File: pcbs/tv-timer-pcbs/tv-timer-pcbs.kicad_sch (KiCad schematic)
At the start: 9 parts, among them J1 Conn_01x03, J2 Conn_01x03

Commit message: Digit ready to go
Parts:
- D1, D2, D3, D4, D5, D6, D7: footprint ProjectLibrary:WS2812b_5mm_THT -> LED_THT:LED_D5.0mm-4_RGB_Wide_Pins
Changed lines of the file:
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@@
 			)
 		)
-		(property "Footprint" "ProjectLibrary:WS2812b_5mm_THT"
+		(property "Footprint" "LED_THT:LED_D5.0mm-4_RGB_Wide_Pins"
 			(at 86.36 57.15 0)
 			(hide yes)
@@
 			)
 		)
-		(property "Footprint" "ProjectLibrary:WS2812b_5mm_THT"
+		(property "Footprint" "LED_THT:LED_D5.0mm-4_RGB_Wide_Pins"
 			(at 193.04 57.15 0)
 			(hide yes)
@@
 			)
 		)
-		(property "Footprint" "ProjectLibrary:WS2812b_5mm_THT"
+		(property "Footprint" "LED_THT:LED_D5.0mm-4_RGB_Wide_Pins"
 			(at 137.16 57.15 0)
 			(hide yes)
@@
 			)
 		)
-		(property "Footprint" "ProjectLibrary:WS2812b_5mm_THT"
+		(property "Footprint" "LED_THT:LED_D5.0mm-4_RGB_Wide_Pins"
 			(at 162.56 57.15 0)
 			(hide yes)
@@
 			)
 		)
-		(property "Footprint" "ProjectLibrary:WS2812b_5mm_THT"
+		(property "Footprint" "LED_THT:LED_D5.0mm-4_RGB_Wide_Pins"
 			(at 111.76 57.15 0)
 			(hide yes)
@@
 			)
 		)
-		(property "Footprint" "ProjectLibrary:WS2812b_5mm_THT"
+		(property "Footprint" "LED_THT:LED_D5.0mm-4_RGB_Wide_Pins"
 			(at 220.98 57.15 0)
 			(hide yes)
@@
 			)
 		)
-		(property "Footprint" "ProjectLibrary:WS2812b_5mm_THT"
+		(property "Footprint" "LED_THT:LED_D5.0mm-4_RGB_Wide_Pins"
 			(at 59.69 57.15 0)
 			(hide yes)

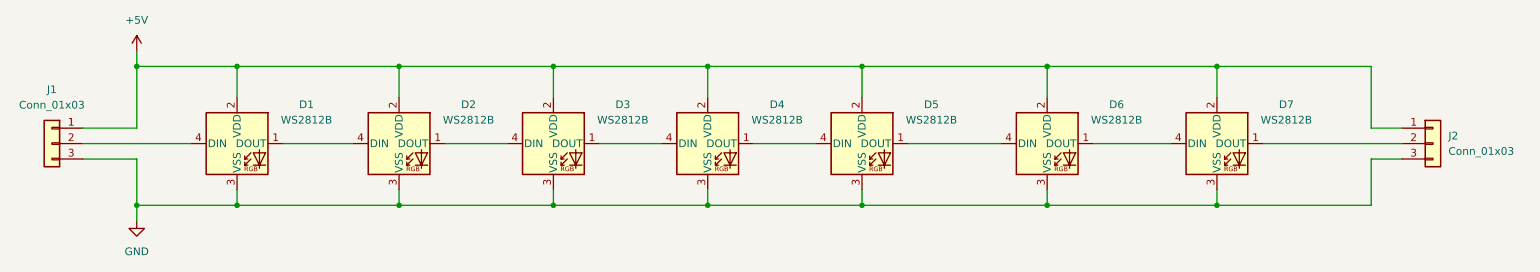
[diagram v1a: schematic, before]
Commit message: ordered
Added other boards and ordered all three
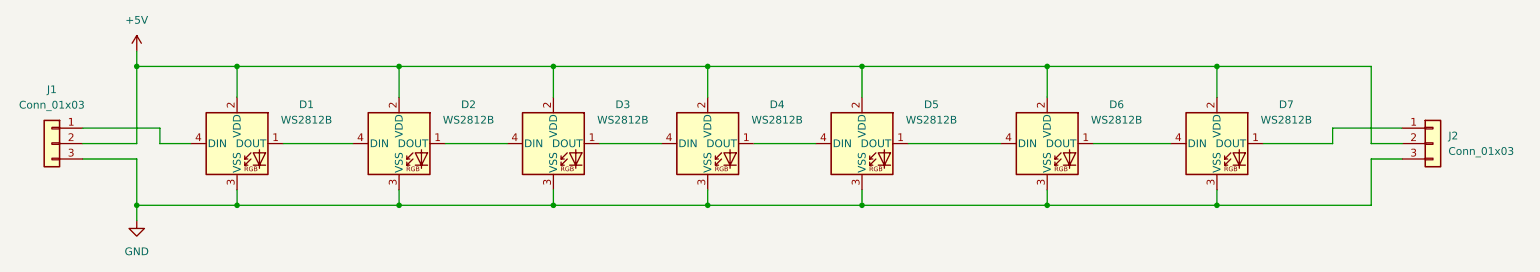
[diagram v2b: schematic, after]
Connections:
- net +5V: now also J1.2 (Pin_2), J2.2 (Pin_2); no longer J1.1 (Pin_1), J2.1 (Pin_1)
- net at D1.4 (DIN): now also J1.1 (Pin_1); no longer J1.2 (Pin_2)
- net at D7.1 (DOUT): now also J2.1 (Pin_1); no longer J2.2 (Pin_2)
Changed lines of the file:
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@@
+	(wire
+		(pts
+			(xy 238.76 49.53) (xy 227.33 49.53)
+		)
+		(stroke
+			(width 0)
+			(type default)
+		)
+	)
+	(wire
+		(pts
+			(xy 245.11 36.83) (xy 245.11 49.53)
+		)
+		(stroke
+			(width 0)
+			(type default)
+		)
+	)
 	(wire
 		(pts
@@
 	(wire
 		(pts
-			(xy 227.33 49.53) (xy 250.19 49.53)
-		)
-		(stroke
-			(width 0)
-			(type default)
-		)
-	)
-	(wire
-		(pts
-			(xy 33.02 49.53) (xy 50.8 49.53)
-		)
-		(stroke
-			(width 0)
-			(type default)
-		)
-	)
-	(wire
-		(pts
 			(xy 41.91 59.69) (xy 58.42 59.69)
 		)
@@
 	(wire
 		(pts
+			(xy 250.19 46.99) (xy 238.76 46.99)
+		)
+		(stroke
+			(width 0)
+			(type default)
+		)
+	)
+	(wire
+		(pts
 			(xy 85.09 36.83) (xy 110.49 36.83)
 		)
@@
 	(wire
 		(pts
-			(xy 245.11 36.83) (xy 245.11 46.99)
-		)
-		(stroke
-			(width 0)
-			(type default)
-		)
-	)
-	(wire
-		(pts
-			(xy 245.11 46.99) (xy 250.19 46.99)
+			(xy 245.11 49.53) (xy 250.19 49.53)
 		)
 		(stroke
@@
 	(wire
 		(pts
+			(xy 238.76 46.99) (xy 238.76 49.53)
+		)
+		(stroke
+			(width 0)
+			(type default)
+		)
+	)
+	(wire
+		(pts
 			(xy 191.77 59.69) (xy 219.71 59.69)
 		)
@@
 	(wire
 		(pts
+			(xy 33.02 49.53) (xy 41.91 49.53)
+		)
+		(stroke
+			(width 0)
+			(type default)
+		)
+	)
+	(wire
+		(pts
 			(xy 110.49 36.83) (xy 135.89 36.83)
 		)
@@
 	(wire
 		(pts
-			(xy 41.91 46.99) (xy 41.91 36.83)
+			(xy 45.72 46.99) (xy 45.72 49.53)
+		)
+		(stroke
+			(width 0)
+			(type default)
+		)
+	)
+	(wire
+		(pts
+			(xy 41.91 36.83) (xy 41.91 49.53)
 		)
 		(stroke
@@
 	(wire
 		(pts
-			(xy 33.02 46.99) (xy 41.91 46.99)
+			(xy 45.72 49.53) (xy 50.8 49.53)
 		)
 		(stroke
@@
 		)
 		(stroke
+			(width 0)
+			(type default)
+		)
+	)
+	(wire
+		(pts
+			(xy 33.02 46.99) (xy 45.72 46.99)
+		)
+		(stroke
